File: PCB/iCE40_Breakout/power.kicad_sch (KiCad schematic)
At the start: 9 parts, among them U3 MIC5504-2.5YM5, U4 MIC5504-1.2YM5, U5 MIC5504-3.3YM5

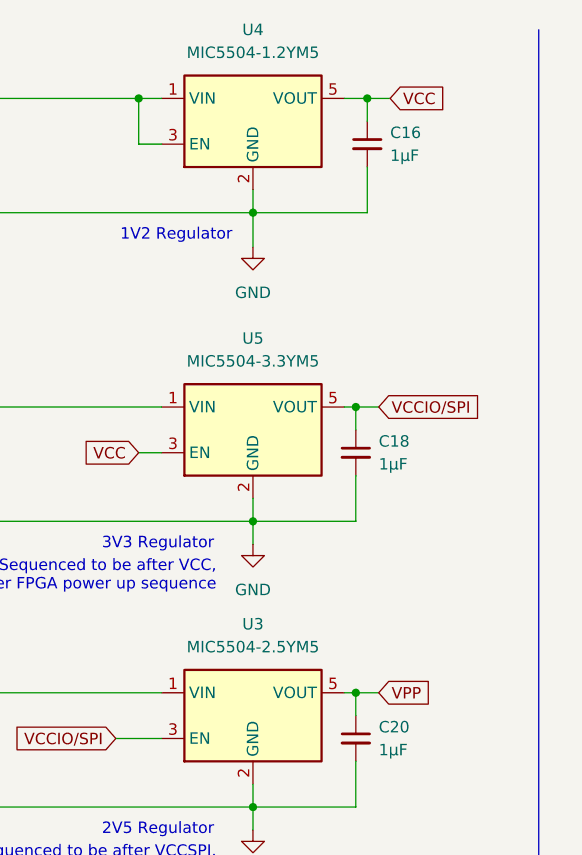
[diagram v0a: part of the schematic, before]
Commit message: Added test points for validating power up sequence
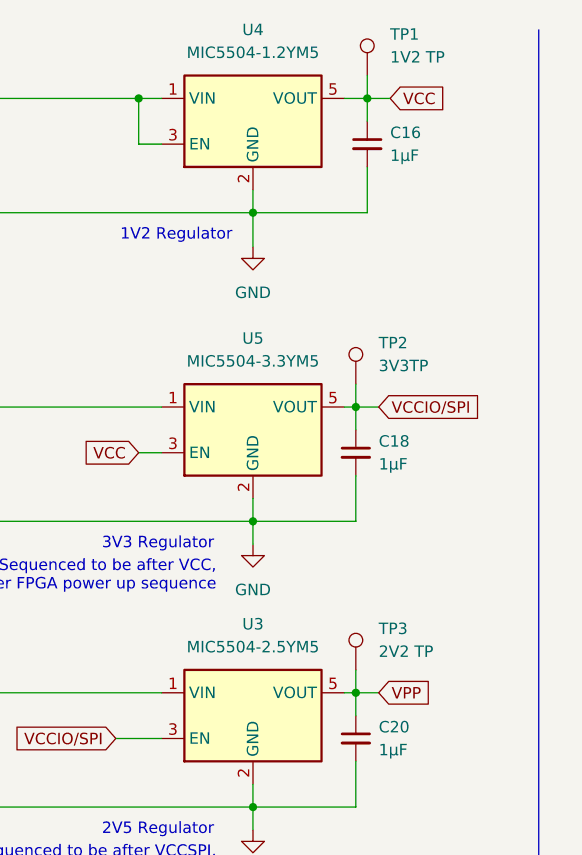
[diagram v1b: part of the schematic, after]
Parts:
- added TP1: 1V2 TP, symbol Connector:TestPoint
- added TP2: 3V3TP, symbol Connector:TestPoint
- added TP3: 2V2 TP, symbol Connector:TestPoint
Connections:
- net VCC: now also TP1.1
- net VCCIO/SPI: now also TP2.1
- net VPP: now also TP3.1
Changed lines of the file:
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@@
+	(wire
+		(pts
+			(xy 80.01 85.09) (xy 80.01 87.63)
+		)
+		(stroke
+			(width 0)
+			(type default)
+		)
+	)
 	(wire
 		(pts
@@
 	(wire
 		(pts
+			(xy 81.28 19.05) (xy 81.28 21.59)
+		)
+		(stroke
+			(width 0)
+			(type default)
+		)
+	)
+	(wire
+		(pts
 			(xy 78.74 55.88) (xy 80.01 55.88)
 		)
@@
 		(pts
 			(xy 78.74 87.63) (xy 80.01 87.63)
+		)
+		(stroke
+			(width 0)
+			(type default)
+		)
+	)
+	(wire
+		(pts
+			(xy 80.01 53.34) (xy 80.01 55.88)
 		)
 		(stroke
@@
 	)
 	(symbol
+		(lib_id "Connector:TestPoint")
+		(at 80.01 85.09 0)
+		(unit 1)
+		(exclude_from_sim no)
+		(in_bom yes)
+		(on_board yes)
+		(dnp no)
+		(property "Reference" "TP3"
+			(at 82.55 80.5179 0)
+			(effects
+				(font
+					(size 1.27 1.27)
+				)
+				(justify left)
+			)
+		)
+		(property "Value" "2V2 TP"
+			(at 82.55 83.0579 0)
+			(effects
+				(font
+					(size 1.27 1.27)
+				)
+				(justify left)
+			)
+		)
+		(property "Footprint" ""
+			(at 85.09 85.09 0)
+			(effects
+				(font
+					(size 1.27 1.27)
+				)
+				(hide yes)
+			)
+		)
+		(property "Datasheet" "~"
+			(at 85.09 85.09 0)
+			(effects
+				(font
+					(size 1.27 1.27)
+				)
+				(hide yes)
+			)
+		)
+		(property "Description" "test point"
+			(at 80.01 85.09 0)
+			(effects
+				(font
+					(size 1.27 1.27)
+				)
+				(hide yes)
+			)
+		)
+		(pin "1"
+		)
+		(instances
+			(project "iCE40_Breakout"
+				(path "/ce4d7974-ef38-4eea-8119-381c4298ef02/01a0af1d-1c95-48f8-8e55-14d3b3651b87"
+					(reference "TP3")
+					(unit 1)
+				)
+			)
+		)
+	)
+	(symbol
 		(lib_id "Regulator_Linear:MIC5504-1.2YM5")
 		(at 68.58 24.13 0)
@@
 	)
 	(symbol
+		(lib_id "Connector:TestPoint")
+		(at 80.01 53.34 0)
+		(unit 1)
+		(exclude_from_sim no)
+		(in_bom yes)
+		(on_board yes)
+		(dnp no)
+		(property "Reference" "TP2"
+			(at 82.55 48.7679 0)
+			(effects
+				(font
+					(size 1.27 1.27)
+				)
+				(justify left)
+			)
+		)
+		(property "Value" "3V3TP"
+			(at 82.55 51.3079 0)
+			(effects
+				(font
+					(size 1.27 1.27)
+				)
+				(justify left)
+			)
+		)
+		(property "Footprint" ""
+			(at 85.09 53.34 0)
+			(effects
+				(font
+					(size 1.27 1.27)
+				)
+				(hide yes)
+			)
+		)
+		(property "Datasheet" "~"
+			(at 85.09 53.34 0)
+			(effects
+				(font
+					(size 1.27 1.27)
+				)
+				(hide yes)
+			)
+		)
+		(property "Description" "test point"
+			(at 80.01 53.34 0)
+			(effects
+				(font
+					(size 1.27 1.27)
+				)
+				(hide yes)
+			)
+		)
+		(pin "1"
+		)
+		(instances
+			(project ""
+				(path "/ce4d7974-ef38-4eea-8119-381c4298ef02/01a0af1d-1c95-48f8-8e55-14d3b3651b87"
+					(reference "TP2")
+					(unit 1)
+				)
+			)
+		)
+	)
+	(symbol
 		(lib_id "power:GND")
 		(at 68.58 71.12 0)
@@
 					(unit 1)
 				)
+			)
+		)
+	)
+	(symbol
+		(lib_id "Connector:TestPoint")
+		(at 81.28 19.05 0)
+		(unit 1)
+		(exclude_from_sim no)
+		(in_bom yes)
+		(on_board yes)
+		(dnp no)
+		(property "Reference" "TP1"
+			(at 83.82 14.4779 0)
+			(effects
+				(font
+					(size 1.27 1.27)
+				)
+				(justify left)
+			)
+		)
+		(property "Value" "1V2 TP"
+			(at 83.82 17.0179 0)
+			(effects
+				(font
+					(size 1.27 1.27)
+				)
+				(justify left)
+			)
+		)
+		(property "Footprint" ""
+			(at 86.36 19.05 0)
+			(effects
+				(font
+					(size 1.27 1.27)
+				)
+				(hide yes)
+			)
+		)
+		(property "Datasheet" "~"
+			(at 86.36 19.05 0)
+			(effects
+				(font
+					(size 1.27 1.27)
+				)
+				(hide yes)
+			)
+		)
+		(property "Description" "test point"
+			(at 81.28 19.05 0)
+			(effects
+				(font
+					(size 1.27 1.27)
+				)
+				(hide yes)
+			)
+		)
+		(pin "1"
+		)
+		(instances
+			(project "iCE40_Breakout"
+				(path "/ce4d7974-ef38-4eea-8119-381c4298ef02/01a0af1d-1c95-48f8-8e55-14d3b3651b87"
+					(reference "TP1")
+					(unit 1)
+				)

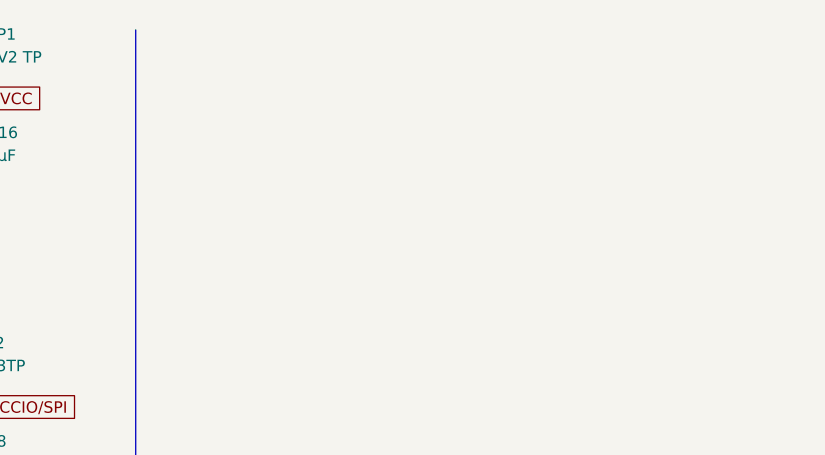
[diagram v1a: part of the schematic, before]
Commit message: Added 3V3 IO rail, reset button, and CDONE LED
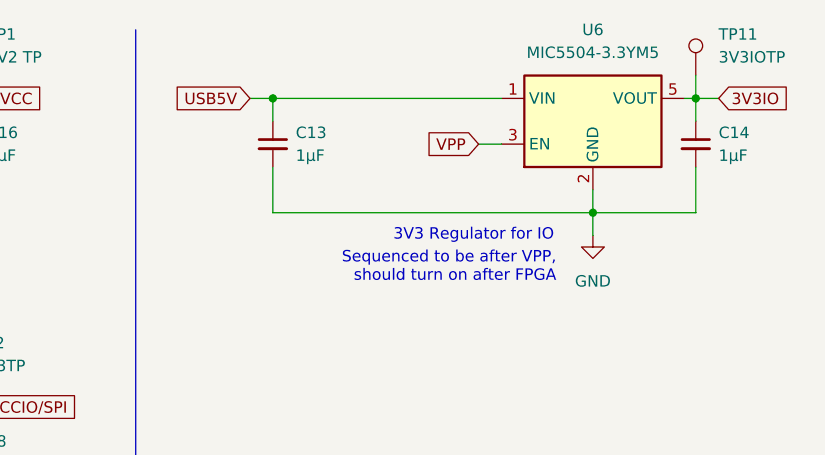
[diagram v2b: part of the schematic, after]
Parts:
- added C13, C14: 1μF, symbol Device:C_Small
- added TP11: 3V3IOTP, symbol Connector:TestPoint
- added U6: MIC5504-3.3YM5, Package_TO_SOT_SMD:SOT-23-5, symbol Regulator_Linear:MIC5504-3.3YM5
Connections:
- net GND: now also C13.2, C14.2, U6.2 (GND)
- net USB5V: now also C13.1, U6.1 (VIN)
- net VPP: now also U6.3 (EN)
- new net 3V3IO: C14.1, TP11.1, U6.5 (VOUT)
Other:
- note added: "3V3 Regulator for IO"
- note added: "Sequenced to be after VPP, should turn on after FPGA"

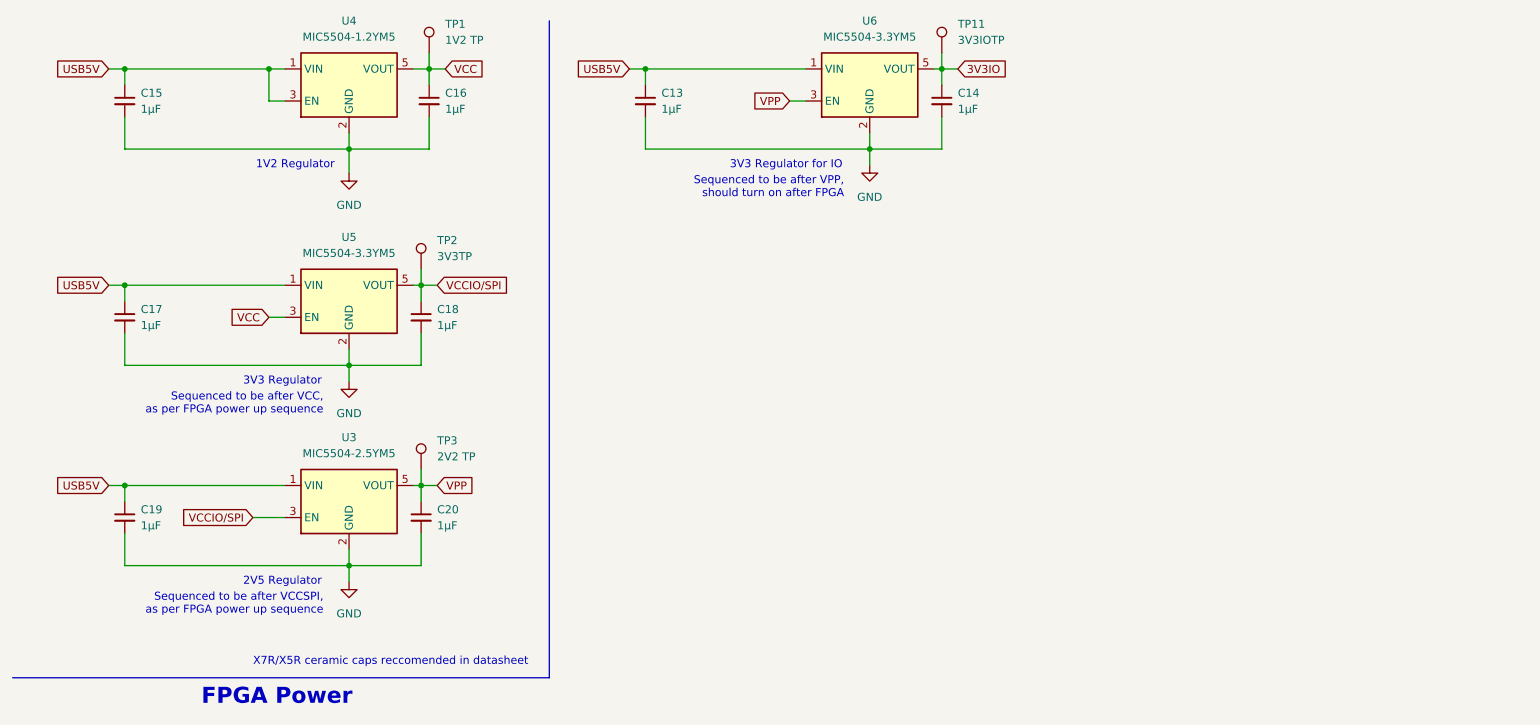
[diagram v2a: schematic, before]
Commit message: Added protection diodes to input power supply
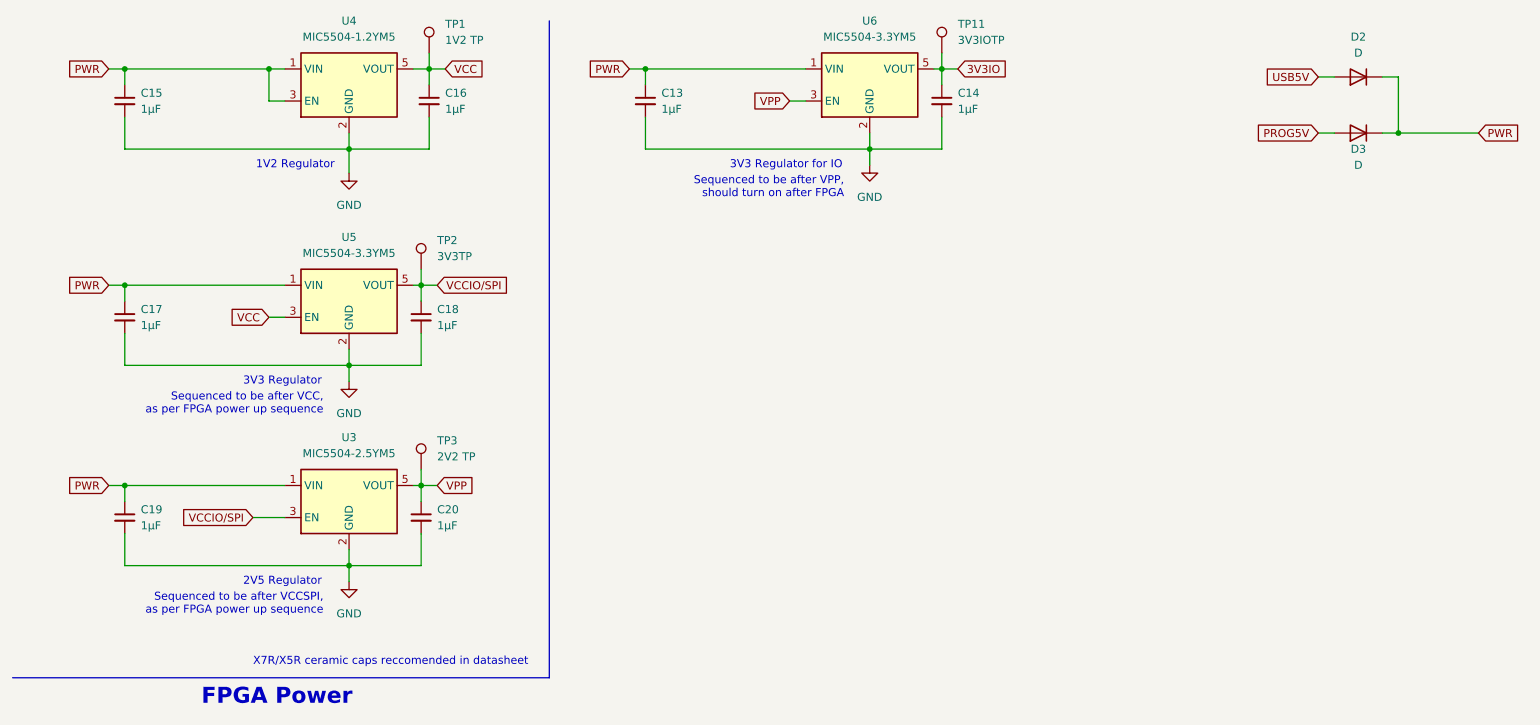
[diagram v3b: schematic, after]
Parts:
- added D2, D3: D, symbol Device:D
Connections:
- net USB5V: now also D2.2 (A); no longer C13.1, C15.1, C17.1, C19.1, U3.1 (VIN), U4.1 (VIN), U4.3 (EN), U5.1 (VIN), U6.1 (VIN)
- new net PROG5V: D3.2 (A)
- new net PWR: C13.1, C15.1, C17.1, C19.1, D2.1 (K), D3.1 (K), U3.1 (VIN), U4.1 (VIN), U4.3 (EN), U5.1 (VIN), U6.1 (VIN)

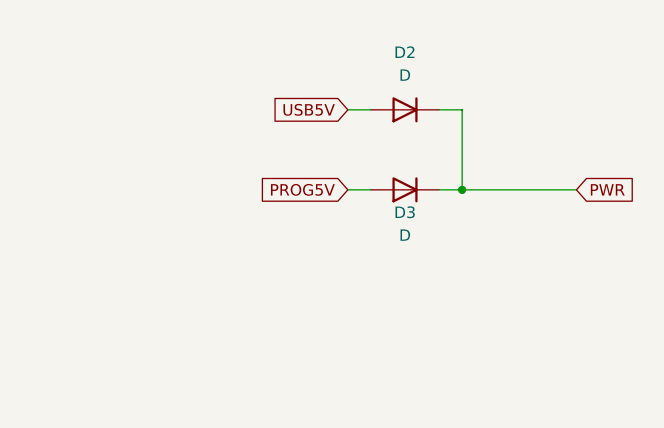
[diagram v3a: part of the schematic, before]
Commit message: Added footprints to all parts, and JLCPCB part numbers
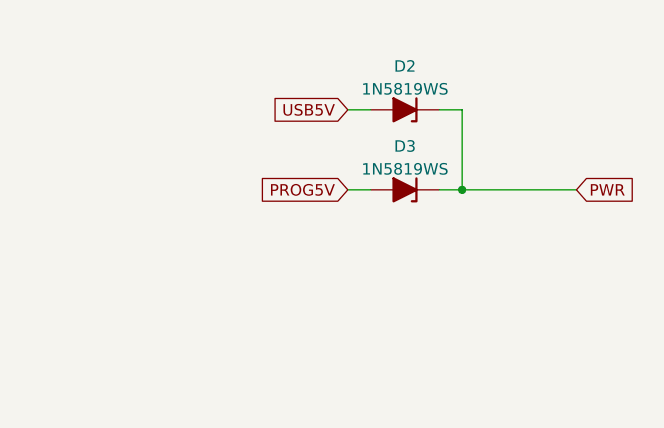
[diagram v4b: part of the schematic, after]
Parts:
- removed D2, D3: D, symbol Device:D
- added D2, D3: 1N5819WS, Diode_SMD:D_SOD-323, symbol Device:D_Zener_Filled
- C13, C14, C15, C16, C17, C18, C19, C20: footprint (none) -> Capacitor_SMD:C_0402_1005Metric; LCSC (none) -> C52923
- TP1, TP11, TP2, TP3: footprint (none) -> TestPoint:TestPoint_Loop_D1.80mm_Drill1.0mm_Beaded
- U3: LCSC (none) -> C626117
- U4: LCSC (none) -> C626115
- U5, U6: LCSC (none) -> C88419
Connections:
- net PROG5V: now also D3.2 (A)
- net PWR: now also D2.1 (K), D3.1 (K)
- net USB5V: now also D2.2 (A)
